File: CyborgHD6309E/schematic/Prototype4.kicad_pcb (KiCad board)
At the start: 2 copper layers, 95 x 72 mm, 26 parts, among them J1 Conn_I2C_Master, J2 Conn_Micro_SD, J3 Conn_USB_Serial, J4 Conn_AVR_UPDI, J5 Conn_AVR_UPDI, SW1 USR_SW, U1 ATmega4809-P, U2 HM628128DLP-5, U3 HD63C09E, U4 ATtiny416-S

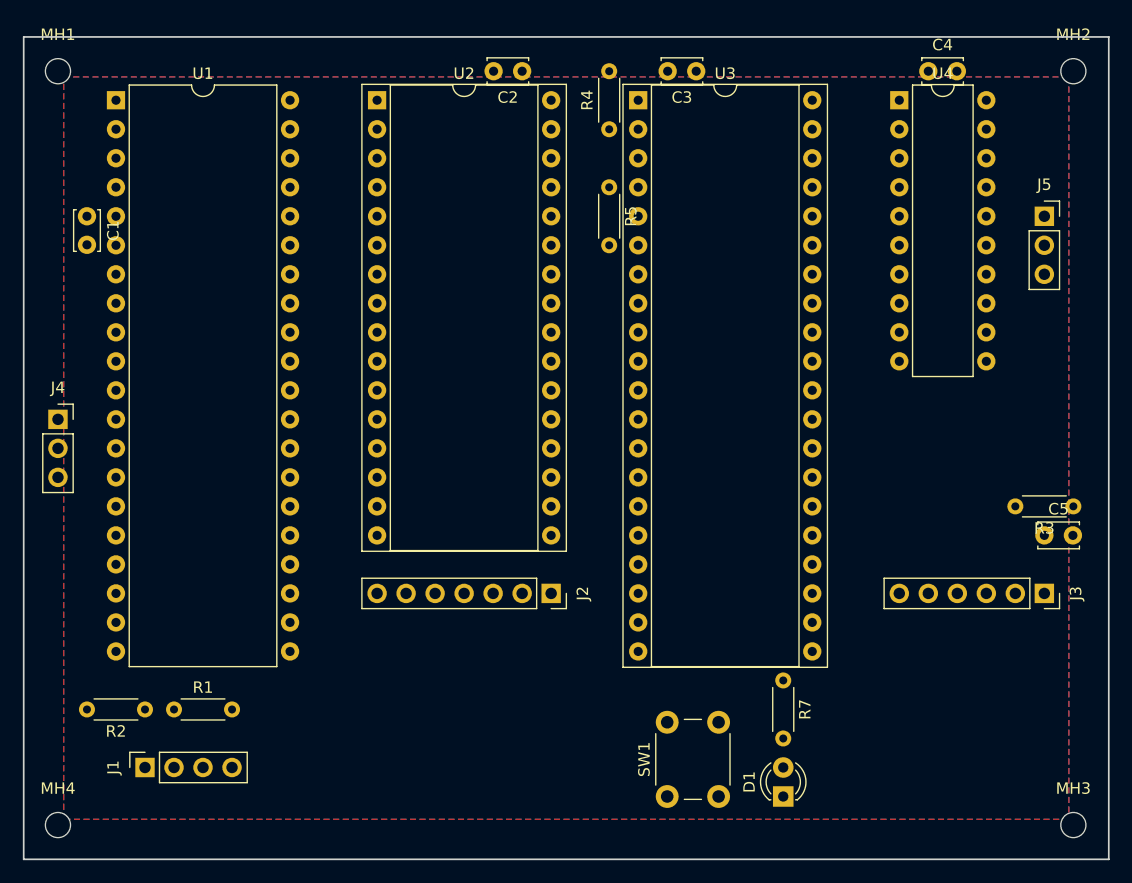
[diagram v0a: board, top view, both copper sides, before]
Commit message: [HD6309E] Use ATtiny414 + 7430 + 74688 for clock generator
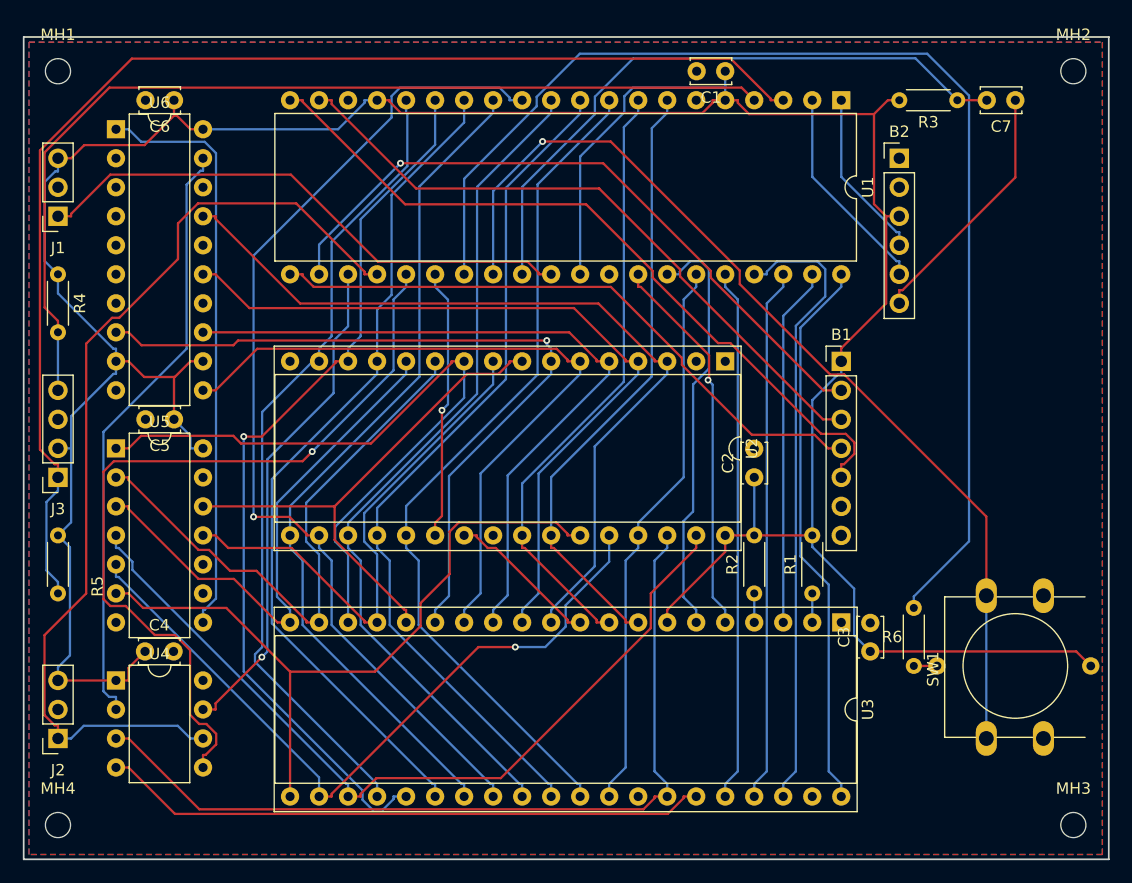
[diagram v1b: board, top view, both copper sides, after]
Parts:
- removed D1: USR_LED, LED_THT:LED_D3.0mm
- removed the J3 at (187.4, 115.7)
- removed J5: Conn_AVR_UPDI, Connector_PinSocket_2.54mm:PinSocket_1x03_P2.54mm_Vertical
- removed the R4 at (149.3, 75.1)
- removed the R5 at (149.3, 80.2)
- removed R7: 560, Resistor_THT:R_Axial_DIN0204_L3.6mm_D1.6mm_P5.08mm_Horizontal
- added B1: Micro_SD, 0-LocalLibrary:uSD_CARD, F.Cu at (169.6, 95.4)
- added B2: USB_Serial, 0-LocalLibrary:GY232V2, F.Cu at (174.7, 77.6)
- added C6: 0.1u, Capacitor_THT:C_Disc_D3.4mm_W2.1mm_P2.50mm, F.Cu at (111.2, 72.5)
- added C7: 0.1u, Capacitor_THT:C_Disc_D3.4mm_W2.1mm_P2.50mm, F.Cu at (184.8, 72.5)
- added R1: 10k, Resistor_THT:R_Axial_DIN0204_L3.6mm_D1.6mm_P5.08mm_Horizontal, F.Cu at (167.0, 115.7)
- added R2: 10k, Resistor_THT:R_Axial_DIN0204_L3.6mm_D1.6mm_P5.08mm_Horizontal, F.Cu at (162.0, 115.7)
- added R6: 560, Resistor_THT:R_Axial_DIN0204_L3.6mm_D1.6mm_P5.08mm_Horizontal, F.Cu at (175.9, 122.1)
- added U5: CD74HCT30, Package_DIP:DIP-14_W7.62mm, F.Cu at (106.1, 103.0)
- added U6: CD74HCT688, Package_DIP:DIP-20_W7.62mm, F.Cu at (106.1, 75.1)
- J2: value Conn_Micro_SD -> Conn_AVR_UPDI; footprint Connector_PinSocket_2.54mm:PinSocket_1x07_P2.54mm_Vertical -> Connector_PinSocket_2.54mm:PinSocket_1x03_P2.54mm_Vertical
- SW1: value USR_SW -> TSD1265; footprint Button_Switch_THT:SW_PUSH_6mm_H5mm -> 0-LocalLibrary:SW_PUSH-LED-12mm
- U4: value ATtiny416-S -> ATtiny412-SS; footprint Package_DIP:DIP-20_W7.62mm -> Package_DIP:DIP-8_W7.62mm
- moved C4 85.3 mm to (108.6, 120.8)
- moved U4 85.3 mm to (106.1, 123.3)
- moved C5 76.9 mm to (111.2, 100.5), turned to 180 degrees
- moved U1 63.5 mm to (169.6, 72.5), turned to 270 degrees
- moved C1 57.3 mm to (159.4, 70.0), turned to 180 degrees
- moved C3 53.0 mm to (172.1, 120.8), turned to 90 degrees
- moved U3 49.1 mm to (169.6, 118.3), turned to 270 degrees
- moved J2 45.0 mm to (101.0, 128.4), turned to 180 degrees
- moved C2 41.0 mm to (162.0, 105.6), turned to 90 degrees
- moved R4 39.4 mm to (101.0, 87.8), turned to 270 degrees
- moved U2 38.1 mm to (159.4, 95.4), turned to 270 degrees
- moved R3 37.0 mm to (179.7, 72.5)
- moved SW1 28.4 mm to (182.3, 128.4)
- moved J3 26.5 mm to (101.0, 105.6), turned to 180 degrees
- moved J1 17.8 mm to (101.0, 82.7), turned to 180 degrees
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- renumbered J4 to J1, J1 to J3, R1 to R4, R2 to R5
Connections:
- C5 pad 1: Net-(C5-Pad1) -> VCC
- C5 pad 2: /~DBG_RST~ -> GND
- J2 pad 1: VCC -> /~ACK
- J2 pad 2: /~SD_CS -> GND
- J2 pad 3: /SD_DI -> VCC
- U1 pad 10: /~IRQ -> /D1
- U1 pad 11: /~USR_SW~ -> /D2
- U1 pad 12: /~INT -> /D3
- U1 pad 13: /~USR_LED~ -> /D4
- U1 pad 14: /~RESET -> /D5
- U1 pad 15: /~ACK -> /D6
- U1 pad 16: /~STEP -> /D7
- U1 pad 23: /BS -> /~INT
- U1 pad 24: /BA -> /~ACK
- U1 pad 25: /LIC -> /~STEP
- U1 pad 26: /AVMA -> /~RAM_E
- U1 pad 27: /RD_WR -> /~USR_LED~
- U1 pad 28: /~RAM_E -> /~USR_SW~
- U1 pad 33: /D0 -> /BS
- U1 pad 34: /D1 -> /BA
- U1 pad 35: /D2 -> /RD_WR
- U1 pad 36: /D3 -> /AVMA
- U1 pad 37: /D4 -> /LIC
- U1 pad 38: /D5 -> /~RESET
- U1 pad 39: /D6 -> /~IRQ
- U1 pad 40: /D7 -> /~HALT
- U1 pad 9: /~HALT -> /D0
- U2 pad 27: /A15 -> /A13
- U2 pad 31: /A13 -> /A15
- U3 pad 33: (no net) -> Net-(U3-Pad33)
- U4 pad 2: /A5 -> Net-(U4-Pad2)
- U4 pad 3: /A10 -> /CLK_E
- U4 pad 4: /A11 -> /CLK_Q
- U4 pad 5: /A12 -> /~STEP
- U4 pad 6: /A4 -> /~ACK
- U4 pad 7: /A6 -> /~INT
- U4 pad 8: /A7 -> GND
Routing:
- net VCC: track 0.00 -> 284.6 mm
- net /SDA: track 0.00 -> 110.4 mm
- net /~USR_LED~: track 0.00 -> 106.0 mm
- net /D3: track 0.00 -> 90.0 mm, vias 0 -> 1
- net /SCL: track 0.00 -> 86.3 mm
- net /~USR_SW~: track 0.00 -> 86.0 mm, vias 0 -> 1
- net /~ACK: track 0.00 -> 85.4 mm
- net /D6: track 0.00 -> 78.9 mm, vias 0 -> 1
- net /CLK_E: track 0.00 -> 75.2 mm
- net /D4: track 0.00 -> 74.8 mm
- net /D1: track 0.00 -> 74.8 mm
- net /D0: track 0.00 -> 74.8 mm
- net /D2: track 0.00 -> 74.8 mm
- net /A15: track 0.00 -> 74.0 mm
- net /D5: track 0.00 -> 74.0 mm
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
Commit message: [CyborgHD6309E] Update pin_maps.h and schematics
- Add DBG_RTS for hard flowcontrol of console.
- Use port A for data bus and port D for controls.
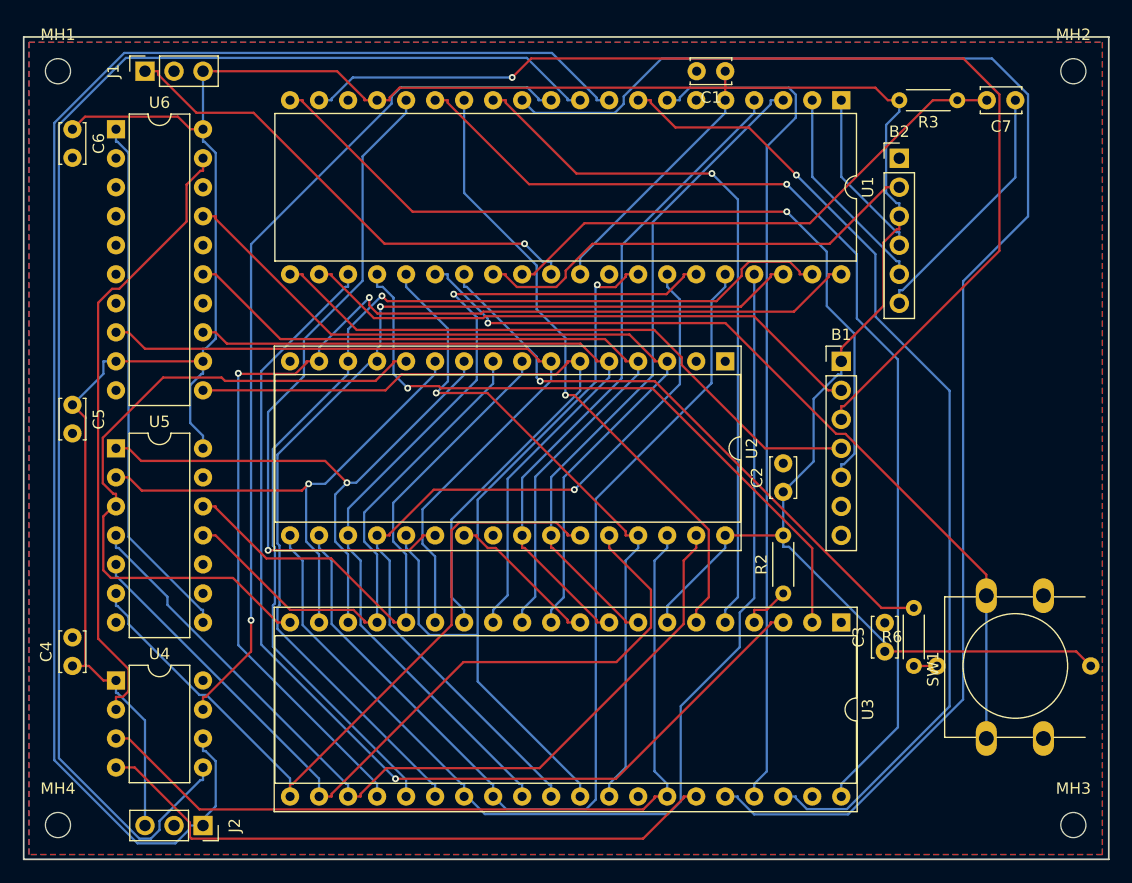
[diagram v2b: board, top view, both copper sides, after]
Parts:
- removed J3: Conn_I2C_Master, Connector_PinSocket_2.54mm:PinSocket_1x04_P2.54mm_Vertical
- removed R1: 10k, Resistor_THT:R_Axial_DIN0204_L3.6mm_D1.6mm_P5.08mm_Horizontal
- removed R4, R5: 4k7, Resistor_THT:R_Axial_DIN0204_L3.6mm_D1.6mm_P5.08mm_Horizontal
- moved J1 14.8 mm to (108.6, 70.0), turned to 90 degrees
- moved J2 14.8 mm to (113.7, 136.0), turned to 270 degrees
- moved C6 9.25 mm to (102.3, 75.1), turned to 270 degrees
- moved C5 8.98 mm to (102.3, 99.2), turned to 270 degrees
- moved C4 6.48 mm to (102.3, 122.1), turned to 90 degrees
- moved C2 2.84 mm to (164.5, 106.8)
- moved R2 2.54 mm to (164.5, 115.7)
- moved C3 1.27 mm to (173.4, 120.8)
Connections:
- net /~DBG_RST~ renamed /~DBG_RESET~
- net /~SD_CS renamed /~SD_CS~
- B1 pad 6: Net-(B1-Pad6) -> (no net)
- B2 pad 2: GND -> /~DBG_RTS~
- J2 pad 1: /~ACK -> /~ACK~
- U1 pad 10: /D1 -> /~STEP~
- U1 pad 11: /D2 -> /~INT~
- U1 pad 12: /D3 -> /AVMA
- U1 pad 13: /D4 -> /BS
- U1 pad 14: /D5 -> /BA
- U1 pad 15: /D6 -> /~HALT~
- U1 pad 16: /D7 -> /~RAM_E~
- U1 pad 23: /~INT -> /~IRQ~
- U1 pad 24: /~ACK -> /~NMI~
- U1 pad 25: /~STEP -> /RD_WR
- U1 pad 26: /~RAM_E -> /~USR_SW~
- U1 pad 28: /~USR_SW~ -> /~DBG_RTS~
- U1 pad 3: /SDA -> /A0
- U1 pad 33: /BS -> /D0
- U1 pad 34: /BA -> /D1
- U1 pad 35: /RD_WR -> /D2
- U1 pad 36: /AVMA -> /D3
- U1 pad 37: /LIC -> /D4
- U1 pad 38: /~RESET -> /D5
- U1 pad 39: /~IRQ -> /D6
- U1 pad 4: /SCL -> /A1
- U1 pad 40: /~HALT -> /D7
- U1 pad 7: /A0 -> /~RESET~
- U1 pad 8: /A1 -> /LIC
- U1 pad 9: /D0 -> /~ACK~
- U2 pad 22: /~RAM_E -> /~RAM_E~
- U3 pad 2: Net-(R1-Pad1) -> /~NMI~
- U3 pad 3: /~IRQ -> /~IRQ~
- U3 pad 33: Net-(U3-Pad33) -> (no net)
- U3 pad 37: /~RESET -> /~RESET~
- U3 pad 40: /~HALT -> /~HALT~
- U4 pad 5: /~STEP -> /~STEP~
- U4 pad 6: /~ACK -> /~ACK~
- U4 pad 7: /~INT -> /~INT~
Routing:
- net /~ACK~: track 0.00 -> 134.5 mm
- net /~STEP~: track 0.00 -> 124.4 mm
- net /SDA: track 110.4 -> 0.00 mm
- net /~HALT~: track 0.00 -> 93.7 mm, vias 0 -> 1
- net /~IRQ~: track 0.00 -> 92.0 mm, vias 0 -> 1
- net /SCL: track 86.3 -> 0.00 mm
- net /~ACK: track 85.4 -> 0.00 mm
- net /AVMA: track 46.6 -> 129.4 mm
- net /~INT~: track 0.00 -> 75.5 mm, vias 0 -> 1
- net /~RESET~: track 0.00 -> 75.1 mm
- net /~STEP: track 70.7 -> 0.00 mm, vias 1 -> 0
- net /~RAM_E~: track 0.00 -> 59.7 mm, vias 0 -> 1
- net /~NMI~: track 0.00 -> 59.2 mm, vias 0 -> 1
- net /~USR_LED~: track 106.0 -> 53.2 mm, vias 0 -> 1
- net /~HALT: track 48.7 -> 0.00 mm
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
